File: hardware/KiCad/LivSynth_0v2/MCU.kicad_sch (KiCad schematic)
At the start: 25 parts, among them J16 USB_B_Micro, J19 SWD, J301 Debug, J302 JTAG, SW7 SW_SPDT, SW8 SW_Push, U9 STM32F405RGT6, Y1 ABM8-16.000MHZ-D1X-T

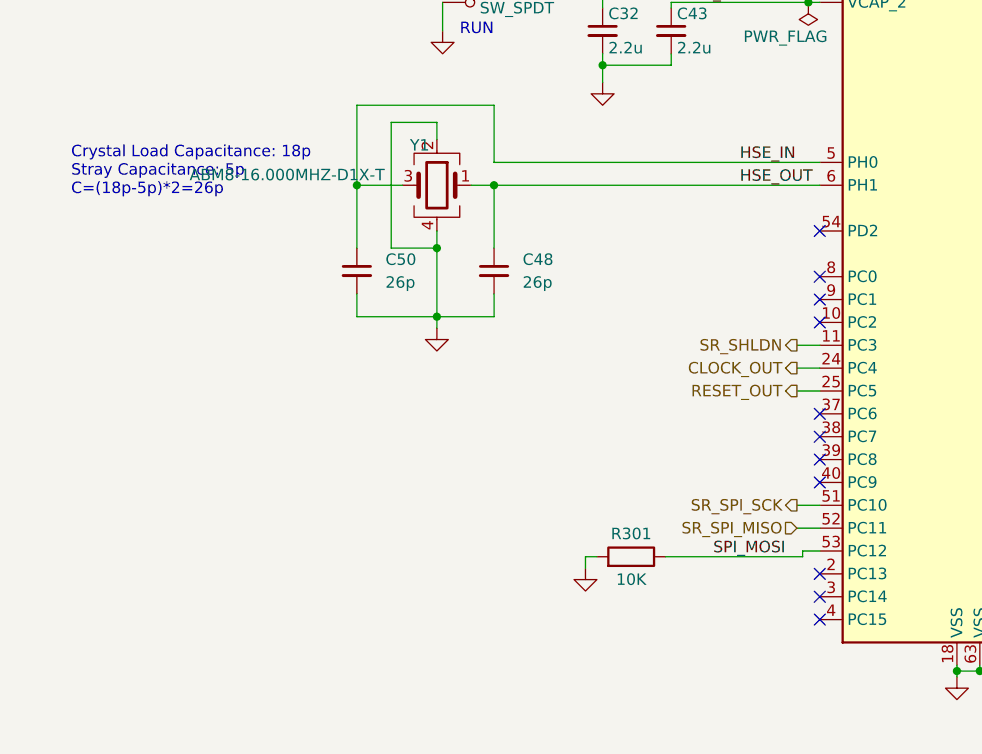
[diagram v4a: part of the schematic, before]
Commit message: LCSC component looked up
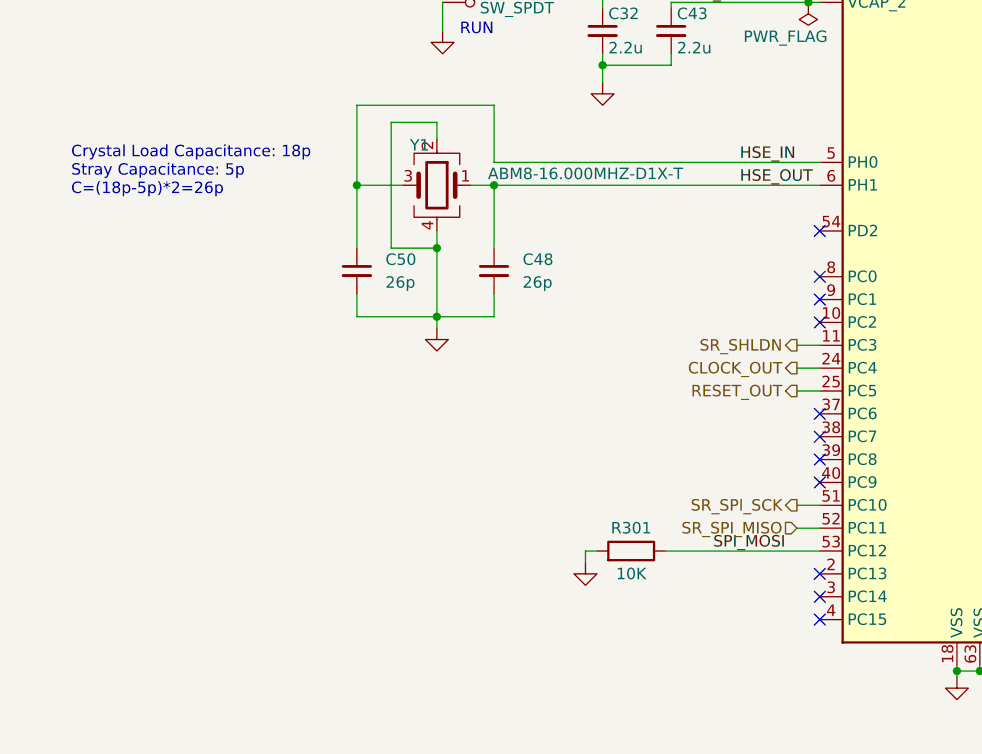
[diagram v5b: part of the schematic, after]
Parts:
- C48, C50: LCSC (none) -> C519484
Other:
- moved on the sheet: R301
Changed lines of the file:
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@@
     (stroke (width 0) (type default) (color 0 0 0 0))
   )
-  (wire (pts (xy 117.475 135.89) (xy 132.715 135.89))
+  (wire (pts (xy 117.475 135.255) (xy 134.62 135.255))
     (stroke (width 0) (type default) (color 0 0 0 0))
   )
@@
     (stroke (width 0) (type default) (color 0 0 0 0))
   )
-  (wire (pts (xy 132.715 135.255) (xy 134.62 135.255))
-    (stroke (width 0) (type default) (color 0 0 0 0))
-  )
   (wire (pts (xy 170.18 140.335) (xy 195.58 140.335))
     (stroke (width 0) (type default) (color 0 0 0 0))
@@
     (stroke (width 0) (type default) (color 0 0 0 0))
   )
-  (wire (pts (xy 108.585 135.89) (xy 108.585 137.16))
+  (wire (pts (xy 108.585 135.255) (xy 108.585 136.525))
     (stroke (width 0) (type default) (color 0 0 0 0))
   )
@@
     (stroke (width 0) (type default) (color 0 0 0 0))
   )
-  (wire (pts (xy 109.855 135.89) (xy 108.585 135.89))
+  (wire (pts (xy 109.855 135.255) (xy 108.585 135.255))
     (stroke (width 0) (type default) (color 0 0 0 0))
   )
@@
   )
   (wire (pts (xy 205.74 94.615) (xy 211.455 94.615))
-    (stroke (width 0) (type default) (color 0 0 0 0))
-  )
-  (wire (pts (xy 132.715 135.89) (xy 132.715 135.255))
     (stroke (width 0) (type default) (color 0 0 0 0))
   )
@@
     (effects (font (size 1.27 1.27)) (justify left bottom))
   )
-  (label "SPI_MOSI" (at 130.81 135.89 180)
+  (label "SPI_MOSI" (at 130.81 135.255 180)
     (effects (font (size 1.27 1.27)) (justify right bottom))
   )
@@
     (pin "1")
   )
-  (symbol (lib_id "Device:R") (at 113.665 135.89 270) (mirror x) (unit 1)
-    (in_bom yes) (on_board yes)
-    (property "Reference" "R301" (id 0) (at 113.665 133.35 90))
-    (property "Value" "10K" (id 1) (at 113.665 138.43 90))
-    (property "Footprint" "Resistor_THT:R_Axial_DIN0207_L6.3mm_D2.5mm_P7.62mm_Horizontal" (id 2) (at 113.665 137.668 90)
-      (effects (font (size 1.27 1.27)) hide)
-    )
-    (property "Datasheet" "~" (id 3) (at 113.665 135.89 0)
+  (symbol (lib_id "Device:R") (at 113.665 135.255 270) (mirror x) (unit 1)
+    (in_bom yes) (on_board yes)
+    (property "Reference" "R301" (id 0) (at 113.665 132.715 90))
+    (property "Value" "10K" (id 1) (at 113.665 137.795 90))
+    (property "Footprint" "Resistor_THT:R_Axial_DIN0207_L6.3mm_D2.5mm_P7.62mm_Horizontal" (id 2) (at 113.665 137.033 90)
+      (effects (font (size 1.27 1.27)) hide)
+    )
+    (property "Datasheet" "~" (id 3) (at 113.665 135.255 0)
       (effects (font (size 1.27 1.27)) hide)
     )
@@
     (in_bom yes) (on_board yes)
     (property "Reference" "Y1" (id 0) (at 90.17 90.17 0))
-    (property "Value" "ABM8-16.000MHZ-D1X-T" (id 1) (at 75.438 93.472 0))
+    (property "Value" "ABM8-16.000MHZ-D1X-T" (id 1) (at 108.585 93.345 0))
     (property "Footprint" "Crystal:Crystal_SMD_3225-4Pin_3.2x2.5mm_HandSoldering" (id 2) (at 92.075 94.615 0)
       (effects (font (size 1.27 1.27)) hide)
@@
       (effects (font (size 1.27 1.27)) hide)
     )
+    (property "LCSC" "C519484" (id 4) (at 98.425 104.14 0)
+      (effects (font (size 1.27 1.27)) hide)
+    )
     (pin "1")
     (pin "2")
@@
       (effects (font (size 1.27 1.27)) hide)
     )
+    (property "LCSC" "C519484" (id 4) (at 83.185 104.14 0)
+      (effects (font (size 1.27 1.27)) hide)
+    )
     (pin "1")
     (pin "2")
@@
     (pin "2")
   )
-  (symbol (lib_id "power:GND") (at 108.585 137.16 0) (mirror y) (unit 1)
-    (in_bom yes) (on_board yes) (fields_autoplaced)
-    (property "Reference" "#PWR0301" (id 0) (at 108.585 143.51 0)
-      (effects (font (size 1.27 1.27)) hide)
-    )
-    (property "Value" "GND" (id 1) (at 108.585 142.24 0)
-      (effects (font (size 1.27 1.27)) hide)
-    )
-    (property "Footprint" "" (id 2) (at 108.585 137.16 0)
-      (effects (font (size 1.27 1.27)) hide)
-    )
-    (property "Datasheet" "" (id 3) (at 108.585 137.16 0)
-      (effects (font (size 1.27 1.27)) hide)
-    )
+  (symbol (lib_id "power:GND") (at 108.585 136.525 0) (mirror y) (unit 1)
+    (in_bom yes) (on_board yes) (fields_autoplaced)
+    (property "Reference" "#PWR0301" (id 0) (at 108.585 142.875 0)
+      (effects (font (size 1.27 1.27)) hide)
+    )
+    (property "Value" "GND" (id 1) (at 108.585 141.605 0)
+      (effects (font (size 1.27 1.27)) hide)
+    )
+    (property "Footprint" "" (id 2) (at 108.585 136.525 0)
+      (effects (font (size 1.27 1.27)) hide)
+    )
+    (property "Datasheet" "" (id 3) (at 108.585 136.525 0)
+      (effects (font (size 1.27 1.27)) hide)
+    )

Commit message: Geographical reannotate
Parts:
- renumbered C37 to C36, C301 to C37, C33 to C38, C32 to C39, C36 to C40, C49 to C41, C45 to C42, C48 to C44, C51 to C45, C43 to C46, C50 to C47, C44 to C48, C46 to C50, C47 to C51, J16 to J21, J301 to J23, J19 to J5, J302 to J6, R301 to R106, R93 to R73, SW8 to SW5, SW7 to SW8
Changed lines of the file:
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@@
   (symbol (lib_id "Connector:Conn_01x02_Male") (at 200.66 140.335 0) (mirror y) (unit 1)
     (in_bom yes) (on_board yes) (fields_autoplaced)
-    (property "Reference" "J301" (id 0) (at 201.93 140.3349 0)
+    (property "Reference" "J23" (id 0) (at 201.93 140.3349 0)
       (effects (font (size 1.27 1.27)) (justify right))
     )
@@
   (symbol (lib_id "Device:C_Small") (at 104.14 50.165 0) (unit 1)
     (in_bom yes) (on_board yes) (fields_autoplaced)
-    (property "Reference" "C36" (id 0) (at 107.315 48.9012 0)
+    (property "Reference" "C40" (id 0) (at 107.315 48.9012 0)
       (effects (font (size 1.27 1.27)) (justify left))
     )
@@
   (symbol (lib_id "Device:C_Small") (at 172.72 49.53 0) (unit 1)
     (in_bom yes) (on_board yes) (fields_autoplaced)
-    (property "Reference" "C37" (id 0) (at 175.26 48.2662 0)
+    (property "Reference" "C36" (id 0) (at 175.26 48.2662 0)
       (effects (font (size 1.27 1.27)) (justify left))
     )
@@
   (symbol (lib_id "Device:C_Small") (at 110.49 77.47 0) (unit 1)
     (in_bom yes) (on_board yes)
-    (property "Reference" "C32" (id 0) (at 111.125 75.565 0)
+    (property "Reference" "C39" (id 0) (at 111.125 75.565 0)
       (effects (font (size 1.27 1.27)) (justify left))
     )
@@
   (symbol (lib_id "Device:R") (at 113.665 135.255 270) (mirror x) (unit 1)
     (in_bom yes) (on_board yes)
-    (property "Reference" "R301" (id 0) (at 113.665 132.715 90))
+    (property "Reference" "R106" (id 0) (at 113.665 132.715 90))
     (property "Value" "10K" (id 1) (at 113.665 137.795 90))
     (property "Footprint" "Resistor_THT:R_Axial_DIN0207_L6.3mm_D2.5mm_P7.62mm_Horizontal" (id 2) (at 113.665 137.033 90)
@@
   (symbol (lib_id "Device:R") (at 120.015 66.675 90) (unit 1)
     (in_bom yes) (on_board yes)
-    (property "Reference" "R93" (id 0) (at 120.015 64.135 90))
+    (property "Reference" "R73" (id 0) (at 120.015 64.135 90))
     (property "Value" "10K" (id 1) (at 120.015 69.215 90))
     (property "Footprint" "Resistor_THT:R_Axial_DIN0207_L6.3mm_D2.5mm_P7.62mm_Horizontal" (id 2) (at 120.015 68.453 90)
@@
   (symbol (lib_id "Device:C_Small") (at 128.27 50.165 0) (unit 1)
     (in_bom yes) (on_board yes) (fields_autoplaced)
-    (property "Reference" "C33" (id 0) (at 131.445 48.9012 0)
+    (property "Reference" "C38" (id 0) (at 131.445 48.9012 0)
       (effects (font (size 1.27 1.27)) (justify left))
     )
@@
   (symbol (lib_id "Connector:Conn_01x06_Male") (at 80.01 170.18 0) (mirror y) (unit 1)
     (in_bom yes) (on_board yes) (fields_autoplaced)
-    (property "Reference" "J19" (id 0) (at 81.28 170.1799 0)
+    (property "Reference" "J5" (id 0) (at 81.28 170.1799 0)
       (effects (font (size 1.27 1.27)) (justify right))
     )
@@
   (symbol (lib_id "Connector:USB_B_Micro") (at 219.075 92.075 0) (mirror y) (unit 1)
     (in_bom yes) (on_board yes) (fields_autoplaced)
-    (property "Reference" "J16" (id 0) (at 226.06 90.8049 0)
+    (property "Reference" "J21" (id 0) (at 226.06 90.8049 0)
       (effects (font (size 1.27 1.27)) (justify right))
     )
@@
   (symbol (lib_id "Device:C_Small") (at 92.075 50.165 0) (unit 1)
     (in_bom yes) (on_board yes) (fields_autoplaced)
-    (property "Reference" "C46" (id 0) (at 95.25 48.9012 0)
+    (property "Reference" "C50" (id 0) (at 95.25 48.9012 0)
       (effects (font (size 1.27 1.27)) (justify left))
     )
@@
   (symbol (lib_id "Device:C_Small") (at 184.785 49.53 0) (unit 1)
     (in_bom yes) (on_board yes) (fields_autoplaced)
-    (property "Reference" "C301" (id 0) (at 187.96 48.2662 0)
+    (property "Reference" "C37" (id 0) (at 187.96 48.2662 0)
       (effects (font (size 1.27 1.27)) (justify left))
     )
@@
   (symbol (lib_id "Device:C_Small") (at 98.425 104.14 0) (unit 1)
     (in_bom yes) (on_board yes) (fields_autoplaced)
-    (property "Reference" "C48" (id 0) (at 101.6 102.8762 0)
+    (property "Reference" "C44" (id 0) (at 101.6 102.8762 0)
       (effects (font (size 1.27 1.27)) (justify left))
     )
@@
   (symbol (lib_id "Connector_Generic:Conn_02x05_Odd_Even") (at 108.585 172.72 0) (unit 1)
     (in_bom yes) (on_board yes) (fields_autoplaced)
-    (property "Reference" "J302" (id 0) (at 109.855 161.29 0))
+    (property "Reference" "J6" (id 0) (at 109.855 161.29 0))
     (property "Value" "JTAG" (id 1) (at 109.855 163.83 0))
     (property "Footprint" "Connector_PinHeader_1.27mm:PinHeader_2x05_P1.27mm_Vertical" (id 2) (at 108.585 172.72 0)
@@
   (symbol (lib_id "Device:C_Small") (at 196.215 49.53 0) (unit 1)
     (in_bom yes) (on_board yes) (fields_autoplaced)
-    (property "Reference" "C49" (id 0) (at 199.39 48.2662 0)
+    (property "Reference" "C41" (id 0) (at 199.39 48.2662 0)
       (effects (font (size 1.27 1.27)) (justify left))
     )
@@
   (symbol (lib_id "Device:C_Small") (at 79.375 50.165 0) (unit 1)
     (in_bom yes) (on_board yes) (fields_autoplaced)
-    (property "Reference" "C44" (id 0) (at 82.55 48.9012 0)
+    (property "Reference" "C48" (id 0) (at 82.55 48.9012 0)
       (effects (font (size 1.27 1.27)) (justify left))
     )
@@
   (symbol (lib_id "Switch:SW_SPDT") (at 97.79 71.755 180) (unit 1)
     (in_bom yes) (on_board yes)
-    (property "Reference" "SW7" (id 0) (at 100.33 69.85 0))
+    (property "Reference" "SW8" (id 0) (at 100.33 69.85 0))
     (property "Value" "SW_SPDT" (id 1) (at 100.965 74.93 0))
     (property "Footprint" "Button_Switch_THT:SW_E-Switch_EG1224_SPDT_Angled" (id 2) (at 97.79 71.755 0)
@@
   (symbol (lib_id "Device:C_Small") (at 116.205 50.165 0) (unit 1)
     (in_bom yes) (on_board yes) (fields_autoplaced)
-    (property "Reference" "C47" (id 0) (at 119.38 48.9012 0)
+    (property "Reference" "C51" (id 0) (at 119.38 48.9012 0)
       (effects (font (size 1.27 1.27)) (justify left))
     )
@@
   (symbol (lib_id "Device:C_Small") (at 79.375 64.77 0) (unit 1)
     (in_bom yes) (on_board yes) (fields_autoplaced)
-    (property "Reference" "C45" (id 0) (at 82.55 63.5062 0)
+    (property "Reference" "C42" (id 0) (at 82.55 63.5062 0)
       (effects (font (size 1.27 1.27)) (justify left))
     )
@@
   (symbol (lib_id "Switch:SW_Push") (at 73.66 64.77 90) (unit 1)
     (in_bom yes) (on_board yes)
-    (property "Reference" "SW8" (id 0) (at 66.675 63.5 90)
+    (property "Reference" "SW5" (id 0) (at 66.675 63.5 90)
       (effects (font (size 1.27 1.27)) (justify right))
     )
@@
   (symbol (lib_id "Device:C_Small") (at 83.185 104.14 0) (unit 1)
     (in_bom yes) (on_board yes) (fields_autoplaced)
-    (property "Reference" "C50" (id 0) (at 86.36 102.8762 0)
+    (property "Reference" "C47" (id 0) (at 86.36 102.8762 0)
       (effects (font (size 1.27 1.27)) (justify left))
     )
@@
   (symbol (lib_id "Device:C_Polarized_Small") (at 67.31 50.165 0) (unit 1)
     (in_bom yes) (on_board yes) (fields_autoplaced)
-    (property "Reference" "C51" (id 0) (at 70.485 48.3488 0)
+    (property "Reference" "C45" (id 0) (at 70.485 48.3488 0)
       (effects (font (size 1.27 1.27)) (justify left))
     )
@@
   (symbol (lib_id "Device:C_Small") (at 118.11 77.47 0) (unit 1)
     (in_bom yes) (on_board yes)
-    (property "Reference" "C43" (id 0) (at 118.745 75.565 0)
-      (effects (font (size 1.27 1.27)) (justify left))
-    )
+    (property "Reference" "C46" (id 0) (at 118.745 75.565 0)
+      (effects (font (size 1.27 1.27)) (justify left))
+    )
